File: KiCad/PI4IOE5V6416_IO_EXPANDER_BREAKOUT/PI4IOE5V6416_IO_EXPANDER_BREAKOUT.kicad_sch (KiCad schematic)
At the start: 15 parts, among them J1 Conn_01x12_Pin, J2 Conn_01x12_Pin, U2 LP5907MFX-3.3, U3 PI4IOE5V6416-TQFN

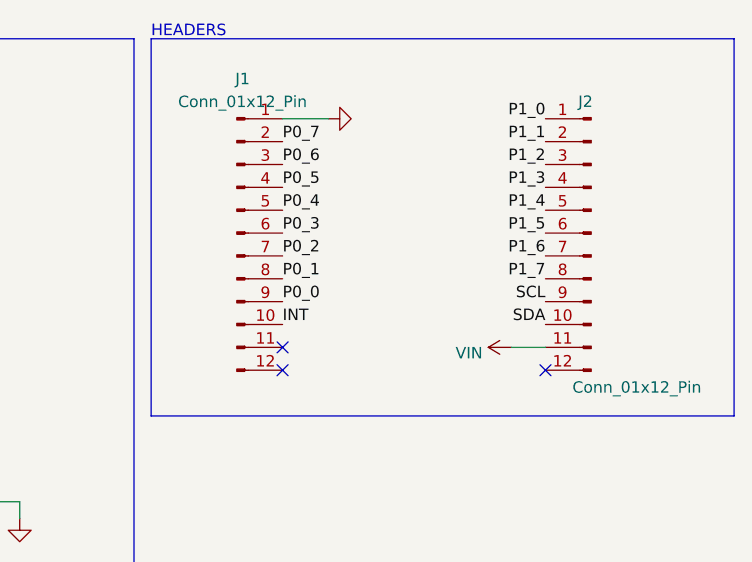
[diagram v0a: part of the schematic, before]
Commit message: Revision 4
- Remove unnecessary pin headers
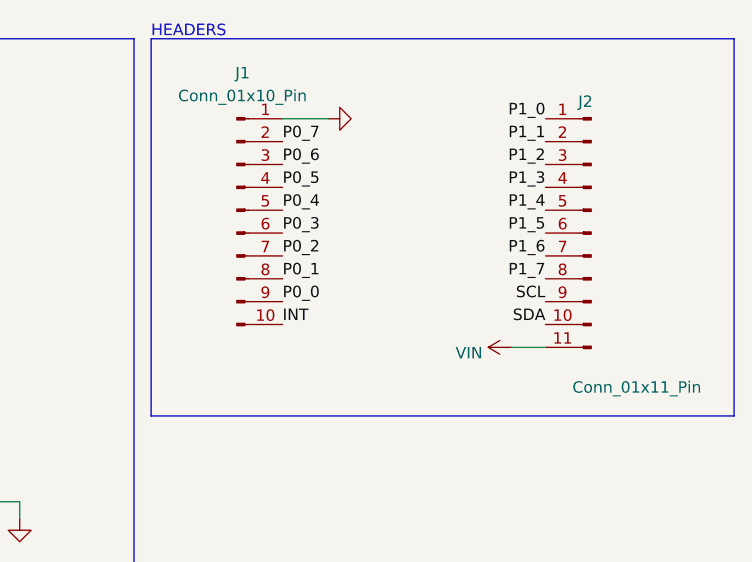
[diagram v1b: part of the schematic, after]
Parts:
- J1: value Conn_01x12_Pin -> Conn_01x10_Pin; footprint Connector_PinHeader_2.54mm:PinHeader_1x12_P2.54mm_Vertical -> Connector_PinHeader_2.54mm:PinHeader_1x10_P2.54mm_Vertical; symbol Connector:Conn_01x12_Pin -> Connector:Conn_01x10_Pin
- J2: value Conn_01x12_Pin -> Conn_01x11_Pin; footprint Connector_PinHeader_2.54mm:PinHeader_1x12_P2.54mm_Vertical -> Connector_PinHeader_2.54mm:PinHeader_1x11_P2.54mm_Vertical; symbol Connector:Conn_01x12_Pin -> Connector:Conn_01x11_Pin
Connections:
- no-connect marks 3 -> 0
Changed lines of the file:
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@@
     (title "PI4IO IO Expander Breakout")
     (date "2023-07-21")
-    (rev "3")
+    (rev "4")
     (company "Playing With Fusion")
     (comment 1 "Designer: Jacob Simeone")
@@
   (junction (at 50.165 116.205) (diameter 0) (color 0 0 0 0)
   )
-  (no_connect (at 209.55 88.9))
-  (no_connect (at 209.55 91.44))
-  (no_connect (at 238.76 91.44))
   (wire (pts (xy 67.945 126.365) (xy 67.945 128.905))
     (stroke (width 0) (type default))
@@
     (effects (font (size 1.27 1.27)) (justify right bottom))
   )
-  (symbol (lib_id "Connector:Conn_01x12_Pin") (at 204.47 76.2 0) (unit 1)
-    (in_bom yes) (on_board yes) (dnp no) (fields_autoplaced)
-    (property "Reference" "J1" (at 205.105 59.0719 0)
-      (effects (font (size 1.27 1.27)))
-    )
-    (property "Value" "Conn_01x12_Pin" (at 205.105 61.6119 0)
-      (effects (font (size 1.27 1.27)))
-    )
-    (property "Footprint" "Connector_PinHeader_2.54mm:PinHeader_1x12_P2.54mm_Vertical" (at 204.47 76.2 0)
-      (effects (font (size 1.27 1.27)) hide)
-    )
-    (property "Datasheet" "~" (at 204.47 76.2 0)
+  (symbol (lib_id "Connector:Conn_01x10_Pin") (at 204.47 73.66 0) (unit 1)
+    (in_bom yes) (on_board yes) (dnp no) (fields_autoplaced)
+    (property "Reference" "J1" (at 205.105 58.42 0)
+      (effects (font (size 1.27 1.27)))
+    )
+    (property "Value" "Conn_01x10_Pin" (at 205.105 60.96 0)
+      (effects (font (size 1.27 1.27)))
+    )
+    (property "Footprint" "Connector_PinHeader_2.54mm:PinHeader_1x10_P2.54mm_Vertical" (at 204.47 73.66 0)
+      (effects (font (size 1.27 1.27)) hide)
+    )
+    (property "Datasheet" "~" (at 204.47 73.66 0)
       (effects (font (size 1.27 1.27)) hide)
     )
     (pin "1")
     (pin "10")
-    (pin "11")
-    (pin "12")
     (pin "2")
     (pin "3")
@@
     )
   )
-  (symbol (lib_id "Connector:Conn_01x12_Pin") (at 243.84 76.2 0) (mirror y) (unit 1)
+  (symbol (lib_id "Connector:Conn_01x11_Pin") (at 243.84 76.2 0) (mirror y) (unit 1)
     (in_bom yes) (on_board yes) (dnp no)
     (property "Reference" "J2" (at 243.205 61.595 0)
       (effects (font (size 1.27 1.27)))
     )
-    (property "Value" "Conn_01x12_Pin" (at 248.92 93.345 0)
-      (effects (font (size 1.27 1.27)))
-    )
-    (property "Footprint" "Connector_PinHeader_2.54mm:PinHeader_1x12_P2.54mm_Vertical" (at 243.84 76.2 0)
+    (property "Value" "Conn_01x11_Pin" (at 248.92 93.345 0)
+      (effects (font (size 1.27 1.27)))
+    )
+    (property "Footprint" "Connector_PinHeader_2.54mm:PinHeader_1x11_P2.54mm_Vertical" (at 243.84 76.2 0)
       (effects (font (size 1.27 1.27)) hide)
     )
@@
     (pin "10")
     (pin "11")
-    (pin "12")
     (pin "2")
     (pin "3")
